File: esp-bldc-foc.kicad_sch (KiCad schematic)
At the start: 9 parts, among them J10 UART, J7 A, J8 B, J9 C

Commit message: finished routing
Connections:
- net UART_RX: now also J10.3 (Pin_3); no longer J10.2 (Pin_2)
- net UART_TX: now also J10.2 (Pin_2); no longer J10.3 (Pin_3)
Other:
- sheet Encoder ports: added ENC_PWM; removed none
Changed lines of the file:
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@@
+    (effects (font (size 1.27 1.27)) (justify right bottom))
+  )
+  (label "ENC_PWM" (at 91.694 90.932 180)
     (effects (font (size 1.27 1.27)) (justify right bottom))
   )
@@
     (effects (font (size 1.27 1.27)) (justify right bottom))
   )
-  (label "ENC_A" (at 72.136 164.846 180)
+  (label "ANALOG_ENC" (at 72.136 164.846 180)
     (effects (font (size 1.27 1.27)) (justify right bottom))
   )
@@
     (effects (font (size 1.27 1.27)) (justify right bottom))
   )
-  (label "AS5055_CS" (at 91.694 90.932 180)
-    (effects (font (size 1.27 1.27)) (justify right bottom))
-  )
-  (label "UART_RX" (at 47.244 104.902 270)
-    (effects (font (size 1.27 1.27)) (justify right bottom))
-  )
-  (label "ENC_B" (at 91.694 83.82 180)
+  (label "UART_RX" (at 44.704 104.902 270)
+    (effects (font (size 1.27 1.27)) (justify right bottom))
+  )
+  (label "ENC_B" (at 91.694 85.598 180)
     (effects (font (size 1.27 1.27)) (justify right bottom))
   )
@@
     (effects (font (size 1.27 1.27)) (justify right bottom))
   )
-  (label "UART_TX" (at 44.704 104.902 270)
+  (label "UART_TX" (at 47.244 104.902 270)
     (effects (font (size 1.27 1.27)) (justify right bottom))
   )
@@
     (effects (font (size 1.27 1.27)) (justify right bottom))
   )
+  (label "ENC_PWM" (at 72.136 167.386 180)
+    (effects (font (size 1.27 1.27)) (justify right bottom))
+  )
   (label "SDA" (at 91.694 71.882 180)
     (effects (font (size 1.27 1.27)) (justify right bottom))
@@
     (effects (font (size 1.27 1.27)) (justify right bottom))
   )
-  (label "ENC_Z" (at 91.694 85.598 180)
+  (label "ENC_Z" (at 91.694 83.82 180)
     (effects (font (size 1.27 1.27)) (justify right bottom))
   )
@@
     )
   )
-  (sheet (at 72.136 141.478) (size 12.954 24.892) (fields_autoplaced)
+  (sheet (at 72.136 141.478) (size 12.954 28.956) (fields_autoplaced)
     (stroke (width 0.1524) (type solid) (color 0 0 0 0))
     (fill (color 0 0 0 0.0000))
@@
       (effects (font (size 1.27 1.27)) (justify left bottom))
     )
-    (property "Sheet file" "Encoder.kicad_sch" (id 1) (at 72.136 166.9546 0)
+    (property "Sheet file" "Encoder.kicad_sch" (id 1) (at 72.136 171.0186 0)
       (effects (font (size 1.27 1.27)) (justify left top))
     )
@@
     )
     (pin "AS5055_CS" input (at 72.136 162.306 180)
+      (effects (font (size 1.27 1.27)) (justify left))
+    )
+    (pin "ENC_PWM" output (at 72.136 167.386 180)
       (effects (font (size 1.27 1.27)) (justify left))
     )
@@
       (reference "#PWR068") (unit 1) (value "+3.3V") (footprint "")
     )
-    (path "/1565b403-cc17-489c-bda8-38a264ef2ff9/3cfc69d7-9950-4148-b339-64561e799e50"
-      (reference "#PWR069") (unit 1) (value "GND") (footprint "")
-    )
     (path "/1565b403-cc17-489c-bda8-38a264ef2ff9/21f7eede-949b-41f1-a4eb-328ad87b2643"
       (reference "#PWR070") (unit 1) (value "GND") (footprint "")
     )
-    (path "/1565b403-cc17-489c-bda8-38a264ef2ff9/6afc1f75-cd7e-49b7-9ac5-a50ac1a47793"
-      (reference "#PWR071") (unit 1) (value "GND") (footprint "")
-    )
     (path "/663bfca8-f474-4636-b91f-0491851dfa21/3ba7f09a-6390-4360-9660-fe17fd957b5c"
       (reference "#PWR072") (unit 1) (value "VBUS") (footprint "")
@@
       (reference "#PWR0119") (unit 1) (value "VBUS") (footprint "")
     )
+    (path "/1565b403-cc17-489c-bda8-38a264ef2ff9/8f1f5b3a-9a47-48d8-a0cd-6787b67e9528"
+      (reference "#PWR0120") (unit 1) (value "GND") (footprint "")
+    )
+    (path "/1565b403-cc17-489c-bda8-38a264ef2ff9/5880819e-9f69-4b56-90a5-ec06062c0b3b"
+      (reference "#PWR0121") (unit 1) (value "GND") (footprint "")
+    )
+    (path "/1565b403-cc17-489c-bda8-38a264ef2ff9/b381266b-c9ab-4a32-8515-54985c64eeeb"
+      (reference "#PWR0122") (unit 1) (value "GND") (footprint "")
+    )
     (path "/0d30d244-1f23-41bf-960a-6073674b9b12/6cca1056-e5f6-41ff-bd5d-af4dbb55249d"
       (reference "AE1") (unit 1) (value "Antenna_Chip") (footprint "2450AT43F0100:ANTC6020X130N")
@@
       (reference "U2") (unit 1) (value "W25Q32JVZP") (footprint "Package_SON:WSON-8-1EP_6x5mm_P1.27mm_EP3.4x4.3mm")
     )
-    (path "/1565b403-cc17-489c-bda8-38a264ef2ff9/a43af72f-222b-48d7-998e-2bd9c1690b08"
-      (reference "U3") (unit 1) (value "AS5055A") (footprint "Package_DFN_QFN:QFN-16-1EP_4x4mm_P0.65mm_EP2.7x2.7mm_PullBack")
+    (path "/1565b403-cc17-489c-bda8-38a264ef2ff9/830d924b-3eb6-48e6-80bf-bd205f577cee"
+      (reference "U3") (unit 1) (value "AS5048B") (footprint "Package_SO:TSSOP-14_4.4x5mm_P0.65mm")
     )
     (path "/663bfca8-f474-4636-b91f-0491851dfa21/4f8d2d8b-0fe1-4ea8-8ecb-4b83c34cccd7"

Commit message: Routing done
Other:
- sheet MCU ports: added IO43, IO44; removed none

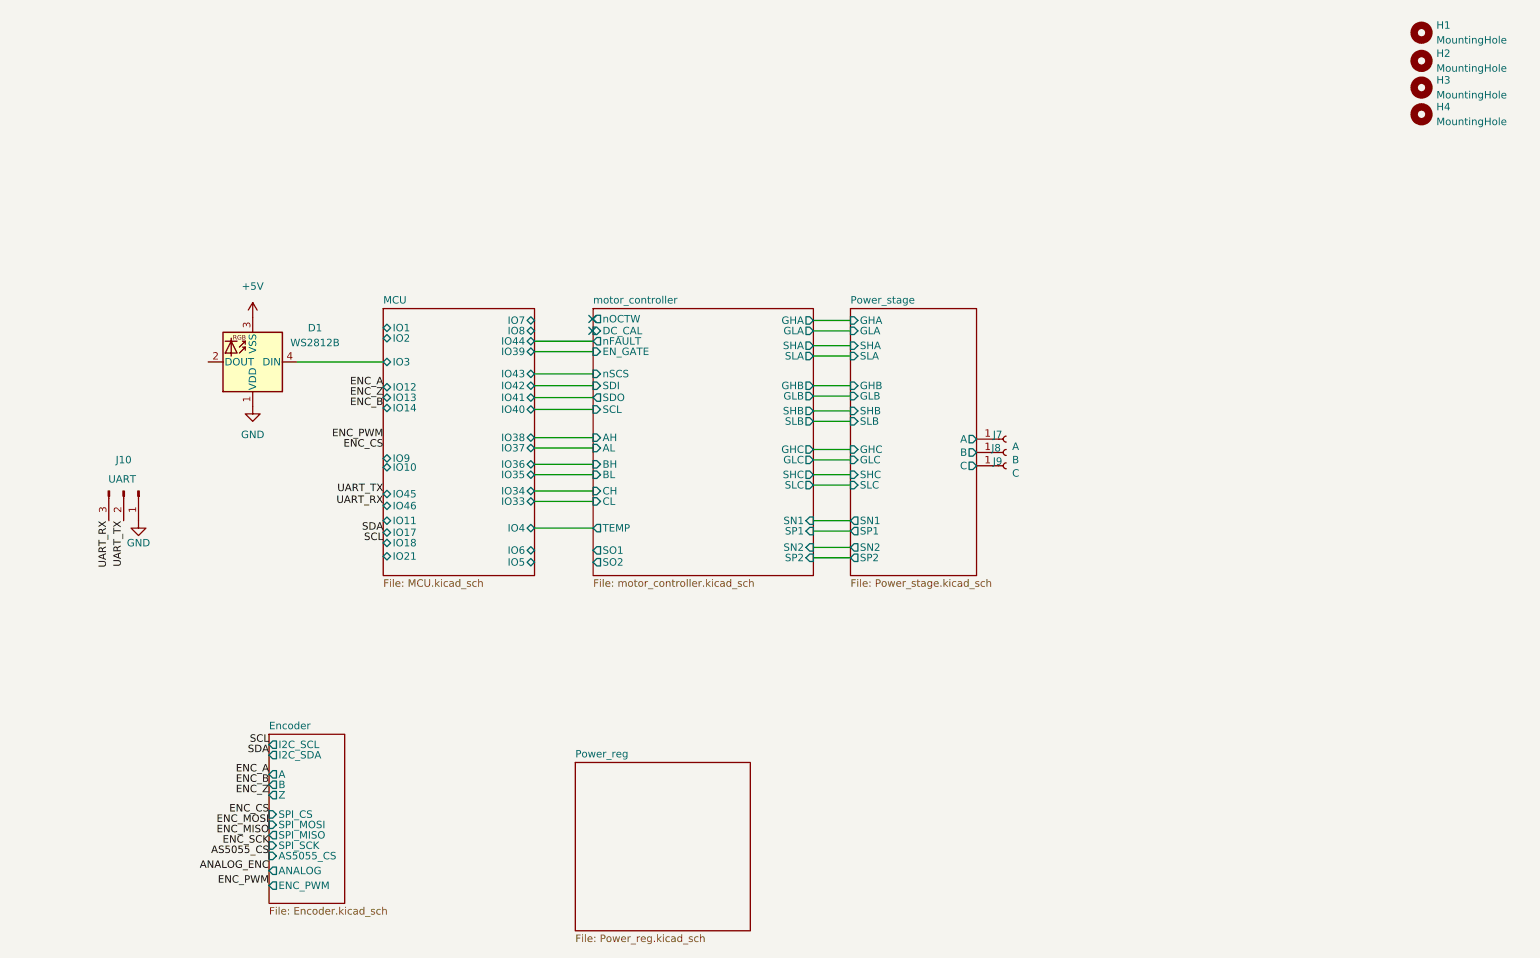
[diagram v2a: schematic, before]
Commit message: Using DRV8353 with built in current sense
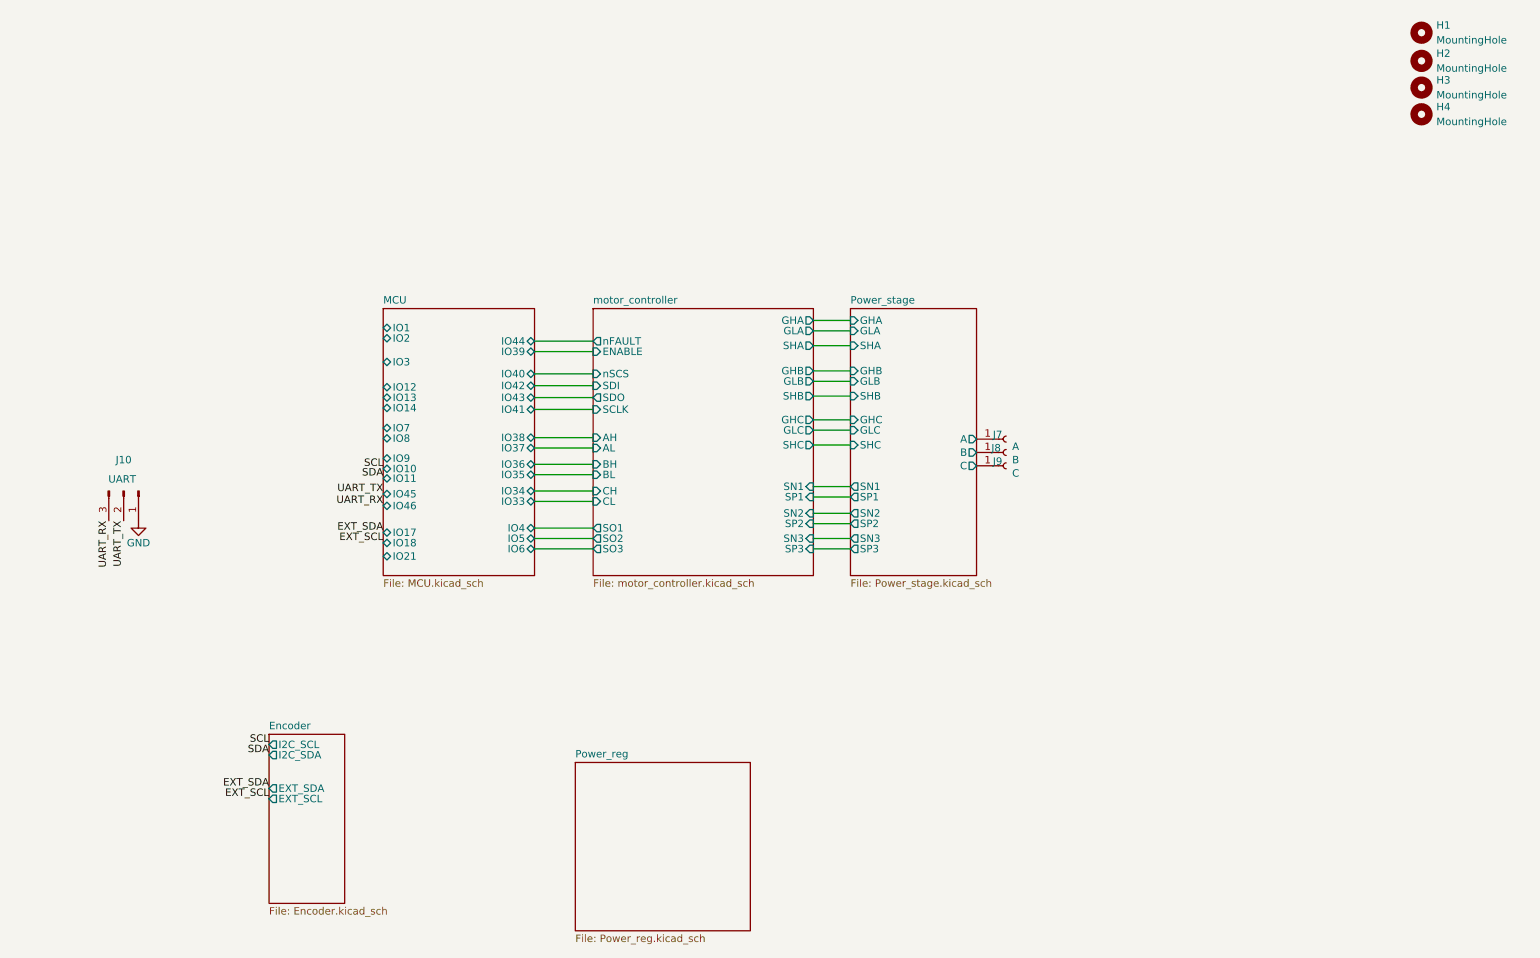
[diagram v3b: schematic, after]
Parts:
- removed D1: WS2812B, LED_SMD:LED_WS2812B_PLCC4_5.0x5.0mm_P3.2mm, symbol LED:WS2812B
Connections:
- no-connect marks 2 -> 0
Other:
- sheet Encoder ports: added EXT_SCL, EXT_SDA; removed A, ANALOG, AS5055_CS, B, ENC_PWM, SPI_CS, SPI_MISO, SPI_MOSI, SPI_SCK, Z
- sheet Power_stage ports: added SN3, SP3; removed SLA, SLB, SLC
- sheet motor_controller ports: added ENABLE, SCLK, SN3, SO3, SP3; removed DC_CAL, EN_GATE, SCL, SLA, SLB, SLC, TEMP, nOCTW

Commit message: init routing done
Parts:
- removed J10: UART, Connector_JST:JST_PH_B3B-PH-K_1x03_P2.00mm_Vertical, symbol Connector:Conn_01x03_Male
- added C25: C, Capacitor_SMD:C_0402_1005Metric, symbol Device:C
- added C45, C47: 470uF, Capacitor_SMD:CP_Elec_10x10, symbol Device:C_Polarized_Small
- added D5: LED, LED_SMD:LED_0603_1608Metric, symbol Device:LED
- added J3: Conn_01x02_Female, Connector_Molex:Molex_CLIK-Mate_502443-0270_1x02-1MP_P2.00mm_Vertical, symbol Connector:Conn_01x02_Female
- added J6: Conn_01x02_Female, Connector_AMASS:AMASS_XT30U-F_1x02_P5.0mm_Vertical, symbol Connector:Conn_01x02_Female
- added NT8: NetTie_2, NetTie:NetTie-2_SMD_Pad2.0mm, symbol Device:NetTie_2
- added R26: 330, Resistor_SMD:R_0402_1005Metric, symbol Device:R
- added U2: MAX3051, Package_SO:SOIC-8_3.9x4.9mm_P1.27mm, symbol Interface_UART:MAX3051
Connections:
- net GND: now also C45.2, C47.2, J6.1 (Pin_1), NT8.2
- net UART_RX: now also U2.4 (RXD)
- net UART_TX: now also U2.1 (TXD)
- new net: D5.2 (A), R26.1
- new net: J3.2 (Pin_2), U2.6 (CANL)
- new net: J3.1 (Pin_1), U2.7 (CANH)
- new net +3.3V: C25.1, U2.3 (VDD)
- new net CAN_RS: U2.8 (RS)
- new net CAN_SD: U2.5 (SHDN)
- new net GNDD: C25.2, D5.1 (K), NT8.1, U2.2 (GND)
- new net MCU/IO19: R26.2
- new net VBUS: C45.1, C47.1, J6.2 (Pin_2)
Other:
- removed sheet Power_reg
- sheet Encoder ports: added U, V, W; removed EXT_SCL, EXT_SDA
- sheet MCU ports: added ADC0, ADC1, ADC2, ADC3, IO0, IO15, IO16, IO19, IO22, IO23, IO24; removed IO21, IO33, IO34, IO35, IO36, IO37, IO38, IO39, IO40, IO41, IO42, IO43, IO44, IO45, IO46
- sheet motor_controller ports: added CAL, GAIN, IDRIVE, MODE, VDS; removed SCLK, SDI, SDO, nSCS

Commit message: designed
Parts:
- removed C45, C47: 470uF, Capacitor_SMD:CP_Elec_10x10, symbol Device:C_Polarized_Small
- added C28, C29, C30, C31, C32, C33: 100uF, Capacitor_SMD:C_1206_3216Metric, symbol Device:C
- added J5: Conn_01x02_Female, Connector_Molex:Molex_CLIK-Mate_502443-0270_1x02-1MP_P2.00mm_Vertical, symbol Connector:Conn_01x02_Female
- C25: value C -> 1uF
- H1, H2, H3, H4, J7, J8, J9: now left out of the parts list
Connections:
- net GND: now also C28.2, C29.2, C30.2, C31.2, C32.2, C33.2
- net VBUS: now also C28.1, C29.1, C30.1, C31.1, C32.1, C33.1
- net at J3.2 (Pin_2), U2.6 (CANL): now also J5.2 (Pin_2)
- net at J3.1 (Pin_1), U2.7 (CANH): now also J5.1 (Pin_1)

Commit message: sarted samd21 layout
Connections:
- net MCU/IO19: no longer R26.2
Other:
- sheet MCU ports: added IO20, IO21, IO27, IO28; removed IO0, IO1, IO24
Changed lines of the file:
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@@
       (effects (font (size 1.27 1.27)) (justify left top))
     )
-    (pin "IO14" bidirectional (at 117.602 79.756 0)
+    (pin "ADC0" input (at 117.602 106.172 0)
       (effects (font (size 1.27 1.27)) (justify right))
     )
-    (pin "IO12" bidirectional (at 117.602 83.82 0)
+    (pin "ADC3" input (at 117.602 112.522 0)
       (effects (font (size 1.27 1.27)) (justify right))
     )
-    (pin "IO13" bidirectional (at 117.602 87.884 0)
-      (effects (font (size 1.27 1.27)) (justify right))
-    )
-    (pin "IO15" bidirectional (at 117.602 81.788 0)
-      (effects (font (size 1.27 1.27)) (justify right))
-    )
-    (pin "IO22" bidirectional (at 91.694 85.852 180)
-      (effects (font (size 1.27 1.27)) (justify left))
-    )
-    (pin "IO23" bidirectional (at 91.694 87.884 180)
-      (effects (font (size 1.27 1.27)) (justify left))
-    )
-    (pin "IO11" bidirectional (at 117.602 75.946 0)
-      (effects (font (size 1.27 1.27)) (justify right))
-    )
-    (pin "IO8" bidirectional (at 117.602 92.456 0)
-      (effects (font (size 1.27 1.27)) (justify right))
-    )
-    (pin "IO9" bidirectional (at 117.602 90.678 0)
-      (effects (font (size 1.27 1.27)) (justify right))
-    )
-    (pin "IO10" bidirectional (at 117.602 85.852 0)
+    (pin "ADC1" input (at 117.602 107.95 0)
       (effects (font (size 1.27 1.27)) (justify right))
     )
@@
       (effects (font (size 1.27 1.27)) (justify right))
     )
-    (pin "ADC3" input (at 91.694 102.362 180)
+    (pin "IO3" bidirectional (at 91.694 70.739 180)
       (effects (font (size 1.27 1.27)) (justify left))
     )
-    (pin "IO6" bidirectional (at 117.602 97.028 0)
+    (pin "IO9" bidirectional (at 91.694 95.8342 180)
+      (effects (font (size 1.27 1.27)) (justify left))
+    )
+    (pin "IO7" bidirectional (at 91.694 90.8558 180)
+      (effects (font (size 1.27 1.27)) (justify left))
+    )
+    (pin "IO6" bidirectional (at 91.694 76.2 180)
+      (effects (font (size 1.27 1.27)) (justify left))
+    )
+    (pin "IO5" bidirectional (at 91.694 74.295 180)
+      (effects (font (size 1.27 1.27)) (justify left))
+    )
+    (pin "IO8" bidirectional (at 91.694 94.1832 180)
+      (effects (font (size 1.27 1.27)) (justify left))
+    )
+    (pin "IO27" bidirectional (at 91.694 109.728 180)
+      (effects (font (size 1.27 1.27)) (justify left))
+    )
+    (pin "IO28" bidirectional (at 91.694 111.4552 180)
+      (effects (font (size 1.27 1.27)) (justify left))
+    )
+    (pin "IO18" bidirectional (at 117.602 90.678 0)
       (effects (font (size 1.27 1.27)) (justify right))
     )
-    (pin "IO4" bidirectional (at 117.602 101.6 0)
+    (pin "IO16" bidirectional (at 117.602 85.852 0)
       (effects (font (size 1.27 1.27)) (justify right))
     )
-    (pin "IO7" bidirectional (at 117.602 95.25 0)
+    (pin "IO21" bidirectional (at 117.602 97.028 0)
       (effects (font (size 1.27 1.27)) (justify right))
     )
-    (pin "IO3" bidirectional (at 91.694 76.2 180)
+    (pin "IO17" bidirectional (at 117.602 87.884 0)
+      (effects (font (size 1.27 1.27)) (justify right))
+    )
+    (pin "IO19" bidirectional (at 117.602 92.456 0)
+      (effects (font (size 1.27 1.27)) (justify right))
+    )
+    (pin "IO20" bidirectional (at 117.602 95.25 0)
+      (effects (font (size 1.27 1.27)) (justify right))
+    )
+    (pin "IO15" bidirectional (at 117.602 83.82 0)
+      (effects (font (size 1.27 1.27)) (justify right))
+    )
+    (pin "IO12" bidirectional (at 117.602 75.946 0)
+      (effects (font (size 1.27 1.27)) (justify right))
+    )
+    (pin "IO10" bidirectional (at 91.694 102.0064 180)
       (effects (font (size 1.27 1.27)) (justify left))
     )
-    (pin "IO1" bidirectional (at 91.694 72.39 180)
+    (pin "IO11" bidirectional (at 117.602 74.168 0)
+      (effects (font (size 1.27 1.27)) (justify right))
+    )
+    (pin "IO14" bidirectional (at 117.602 81.788 0)
+      (effects (font (size 1.27 1.27)) (justify right))
+    )
+    (pin "IO13" bidirectional (at 117.602 79.756 0)
+      (effects (font (size 1.27 1.27)) (justify right))
+    )
+    (pin "IO2" bidirectional (at 103.124 114.3 270)
       (effects (font (size 1.27 1.27)) (justify left))
     )
-    (pin "IO2" bidirectional (at 91.694 74.295 180)
+    (pin "IO4" bidirectional (at 91.694 72.39 180)
       (effects (font (size 1.27 1.27)) (justify left))
     )
-    (pin "IO0" bidirectional (at 91.694 70.739 180)
-      (effects (font (size 1.27 1.27)) (justify left))
-    )
-    (pin "IO16" bidirectional (at 117.602 74.168 0)
+    (pin "IO22" bidirectional (at 117.602 99.822 0)
       (effects (font (size 1.27 1.27)) (justify right))
     )
-    (pin "IO17" bidirectional (at 91.694 81.026 180)
-      (effects (font (size 1.27 1.27)) (justify left))
-    )
-    (pin "ADC1" input (at 117.602 107.95 0)
+    (pin "IO23" bidirectional (at 117.602 101.6 0)
       (effects (font (size 1.27 1.27)) (justify right))
     )
-    (pin "IO18" bidirectional (at 91.694 82.677 180)
-      (effects (font (size 1.27 1.27)) (justify left))
-    )
-    (pin "IO19" bidirectional (at 91.694 98.552 180)
-      (effects (font (size 1.27 1.27)) (justify left))
-    )
-    (pin "IO24" bidirectional (at 91.694 89.916 180)
-      (effects (font (size 1.27 1.27)) (justify left))
-    )
-    (pin "ADC0" input (at 117.602 106.172 0)
-      (effects (font (size 1.27 1.27)) (justify right))
-    )
-    (pin "IO5" bidirectional (at 117.602 99.822 0)
-      (effects (font (size 1.27 1.27)) (justify right))
-    )
